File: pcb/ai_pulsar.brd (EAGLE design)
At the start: 30.5 x 30.5 mm, 24 parts, among them IC1 DS1307SO8-TIGHT, IC2 74HCT245MTC, J1 JST-3-MALE, J2 1X05, U1 MIC5205-3.3

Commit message: minor silkscreen fix
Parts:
- J1: value JST-3-MALE -> JST-3P-MALE
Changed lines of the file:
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@@
 <attribute name="NAME" x="22.70684375" y="7.712009375" size="0.8128" layer="26" ratio="10" rot="MR42"/>
 </element>
-<element name="J1" library="Ai_Connectors" package="JST-3P-SMD" value="JST-3-MALE" x="25.0952" y="15.24" smashed="yes" rot="MR90"/>
+<element name="J1" library="Ai_Connectors" package="JST-3P-SMD" value="JST-3P-MALE" x="25.0952" y="15.24" smashed="yes" rot="MR90"/>
 <element name="-" library="Ai_Connectors" package="1X01-PETAL" value="1X01-PETAL" x="6.985" y="25.4" smashed="yes" rot="R40"/>
 <element name="+" library="Ai_Connectors" package="1X01-PETAL" value="1X01-PETAL" x="15.494" y="2.032" smashed="yes" rot="R180"/>

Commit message: Updating
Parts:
- added C5: 100uF, Ai_Passives:CAP-POL-EIA3216
- D1: device Ai_DiscreteSemis:SOD-523 -> Ai_DiscreteSemis:SMA-403D
- U1: value MIC5205-3.3 -> MIC5219-3.3
- moved U$6 11.0 mm to (23.8, 23.6)
- moved D1 8.71 mm to (13.1, 27.3), flipped to the bottom, turned to 222 degrees
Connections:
- net 5V: now also C5.A
- net GND: now also C5.C
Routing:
- net N$5: track 8.68 -> 18.2 mm, vias 2 -> 1
- net 5V: track 57.3 -> 63.5 mm
- net N$1: track 18.8 -> 19.5 mm
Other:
- board text added: "v1.2"
- board text removed: "v1.1"

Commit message: updating
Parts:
- removed +, -, D: 1X01-PETAL, Ai_Connectors:1X01-PETAL
- removed D1: PMEG2010AEB, Ai_DiscreteSemis:SMA-403D
- removed IC2: 74HCT245MTC, Ai_IC:SSOP20
- added C10, C11, C12, C13, C14, C15, C16, C17, C18, C19, C20, C21, C22, C23, C24, C25, C26, C27, C28, C29, C6, C7, C8, C9: (no value), Ai_Passives:CAP-0603
- added F1: (no value), Ai_Passives:PTC-1206
- added JS1: 1X02-SJ-NO, Ai_Connectors:1X02-SJ-NO
- added JS2: 1X02-SJ-NC, Ai_Connectors:1X02-SJ-NC
- added LED1, LED10, LED11, LED12, LED13, LED14, LED15, LED16, LED17, LED18, LED19, LED2, LED20, LED21, LED22, LED23, LED24, LED3, LED4, LED5, LED6, LED7, LED8, LED9: LED-WS2812B-SM, Ai_LED:LED-WS2812B-SM
- added LED25, LED26: (no value), Ai_LED:LED-0603
- added Q1: BSS138, Ai_DiscreteSemis:SOT-23
- added R10, R11: 330, Ai_Passives:RES-0603
- added R6: 10K, Ai_Passives:RES-0603
- added R7, R8, R9: 1K, Ai_Passives:RES-0603
- added STANDOFF1, STANDOFF2, STANDOFF3, STANDOFF4: STAND-OFF4T, Ai_Electromechanical:STAND-OFF-4T
- added U2: FT231X-Q, Ai_IC:QFN20
- C1, C3: value 0.1uF -> 10uF
- C2: value 10uF -> 0.1uF
- C4: value 10uF -> (none)
- C5: value 100uF -> (none); device Ai_Passives:CAP-POL-EIA3216 -> Ai_Passives:CAP-0603
- J2: value 1X05 -> JST-2P-MALE; device Ai_Connectors:1X05 -> Ai_Connectors:JST-2P-SMD
- R1, R2: value 1K -> 22
- R5: value 1K -> 10K
- moved J2 50.0 mm to (52.7, 26.0), turned to 0 degrees
- moved USB1 49.7 mm to (38.9, 48.3), turned to 180 degrees
- moved C5 40.2 mm to (16.0, 45.2), flipped to the top, turned to 0 degrees
- moved J1 38.9 mm to (52.7, 42.7), flipped to the top, turned to 180 degrees
- moved C3 35.9 mm to (42.7, 22.9), turned to 270 degrees
- moved R1 35.9 mm to (28.4, 45.2), turned to 0 degrees
- moved R2 35.1 mm to (28.4, 43.7), turned to 0 degrees
- moved R3 32.8 mm to (45.7, 22.9), turned to 90 degrees
- moved C4 28.4 mm to (16.0, 43.7)
- moved C2 28.1 mm to (16.5, 39.4), turned to 270 degrees
- moved R4 26.6 mm to (18.0, 39.4)
- moved IC1 23.9 mm to (16.5, 30.5), flipped to the top, turned to 270 degrees
- moved C1 22.6 mm to (15.0, 39.4), turned to 90 degrees
- moved 3V-BATT 20.7 mm to (33.0, 17.8), flipped to the top, turned to 180 degrees
- moved U$6 20.7 mm to (34.3, 5.71), turned to 0 degrees
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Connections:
- removed net 3V3IO3: RFDUINO.4
- removed net 3V3IO4: RFDUINO.5
- removed net DTR: C1.2, J2.5
- removed net RESET: C1.1, RFDUINO.14
- removed net RXI: J2.4, R1.2
- removed net TXO: J2.3, R2.2
- new net !RST: C5.1, RFDUINO.14
- new net N$10: C5.2, U2.18
- new net N$11: LED26.C, R11.2
- new net N$12: LED25.C, R10.2
- new net N$14: R10.1, U2.14
- new net N$15: R11.1, U2.7
- new net N$17: JS1.2
- new net N$2: R1.2, USB1.D-
- new net N$30: JS2.1, LED1.4
- new net N$31: LED1.2, LED2.4
- new net N$6: R2.2, USB1.D+
- new net N$7: R9.1, U2.1
- new net N$8: R8.1, U2.17
- new net USBDM: R1.1, U2.9
- new net USBDP: R2.1, U2.8
- new net VCCIO: C4.2, LED25.A, LED26.A, U2.10, U2.11, U2.20
- net 3V3: now also C2.2, C3.1, Q1.1, R5.1; no longer C3.2, C4.1
- net 3V3IO2: now also Q1.2, R5.2; no longer IC2.2
- net 3V3IO5: no longer RFDUINO.6
- net 3V3IO6: no longer RFDUINO.7
- net 3V3RXD: now also R9.2; no longer R1.1
- net 3V3TXD: now also R8.2; no longer R2.1
- net 5V: now also C1.1, C6.2, C7.2, F1.2, LED1.1, LED2.1, LED3.1, R6.1, U2.12; no longer +.1, C2.1, C5.A, D1.C, IC2.1, IC2.20, J2.2
- net 5VIO2: now also Q1.3, R6.2, R7.2; no longer IC2.18, R5.2
- net D: now also JS1.1, JS2.2, R7.1; no longer D.1, R5.1
- net GND: now also C1.2, C2.1, C3.2, C4.1, C6.1, C7.1, LED1.3, LED2.3, U2.13, U2.21, U2.3; no longer -.1, C2.2, C3.1, C4.2, C5.C, IC2.10, IC2.19, J2.1
- net N$5: now also F1.1; no longer D1.A
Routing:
- net 5V: track 63.5 -> 0.00 mm, vias 4 -> 0
- net 3V3: track 31.2 -> 0.00 mm
- net 3V3IO6: track 26.5 -> 0.00 mm, vias 2 -> 0
- net 3V3IO5: track 24.3 -> 0.00 mm, vias 2 -> 0
- net N$1: track 19.5 -> 0.00 mm
- net 3V3IO2: track 19.5 -> 0.00 mm, vias 2 -> 0
- net 3V3TXD: track 18.4 -> 0.00 mm, vias 2 -> 0
- net N$5: track 18.2 -> 0.00 mm, vias 1 -> 0
- net N$4: track 17.5 -> 0.00 mm, vias 1 -> 0
- net D: track 17.1 -> 0.00 mm, vias 1 -> 0
- net DTR: track 13.2 -> 0.00 mm
- net RXI: track 11.6 -> 0.00 mm, vias 1 -> 0
- net 5VIO2: track 10.8 -> 0.00 mm
- net TXO: track 9.90 -> 0.00 mm
- net N$3: track 8.91 -> 0.00 mm, vias 1 -> 0
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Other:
- board size 30.5 x 30.5 mm -> 66 x 66 mm

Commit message: routing under way
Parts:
- added D1: DIODE-SCHOTTKY-DUAL, Ai_DiscreteSemis:SOT-23
- added D2: (no value), Ai_DiscreteSemis:SOD-523
- 3V-BATT: device Ai_Connectors:CR1220-SMD -> Ai_Connectors:CR1025-SMD
- moved C29 139.8 mm to (37.1, 63.9), turned to 82.5 degrees
- moved C28 139.0 mm to (29.0, 63.9), turned to 97.5 degrees
- moved C27 136.2 mm to (21.1, 61.8), turned to 112.5 degrees
- moved C26 126.1 mm to (14.1, 57.7), turned to 127.5 degrees
- moved C25 120.3 mm to (8.33, 52.0), turned to 142.5 degrees
- moved C24 113.3 mm to (4.27, 44.9), turned to 157.5 degrees
- moved C9 106.5 mm to (61.8, 44.9), turned to 22.5 degrees
- moved C10 104.8 mm to (63.9, 37.1), turned to 7.5 degrees
- moved C11 101.6 mm to (63.9, 29.0), turned to 352.5 degrees
- moved C23 101.2 mm to (2.16, 37.1), turned to 172.5 degrees
- moved C12 97.2 mm to (61.8, 21.1), turned to 337.5 degrees
- moved C22 93.2 mm to (2.16, 29.0), turned to 187.5 degrees
- moved C13 86.3 mm to (57.7, 14.1), turned to 322.5 degrees
- moved C21 85.8 mm to (4.27, 21.1), turned to 202.5 degrees
- moved C14 84.0 mm to (52.0, 8.33), turned to 307.5 degrees
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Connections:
- new net +: D2.A, J2.1
- new net DI-1: LED6.2, LED7.4
- new net DI-2: LED18.2, LED19.4
- new net N$13: LED12.2, LED13.4
- new net N$16: LED2.2, LED3.4
- new net N$18: LED3.2, LED4.4
- new net N$19: LED4.2, LED5.4
- new net N$20: LED5.2, LED6.4
- new net N$21: LED7.2, LED8.4
- new net N$22: LED8.2, LED9.4
- new net N$23: LED10.4, LED9.2
- new net N$24: LED10.2, LED11.4
- new net N$25: LED11.2, LED12.4
- new net N$26: LED13.2, LED14.4
- new net N$27: LED14.2, LED15.4
- new net N$28: LED15.2, LED16.4
- new net N$29: LED16.2, LED17.4
- new net N$32: LED17.2, LED18.4
- new net N$33: LED19.2, LED20.4
- new net N$34: LED20.2, LED21.4
- new net N$35: LED21.2, LED22.4
- new net N$36: LED22.2, LED23.4
- new net N$37: LED23.2, LED24.4
- new net VBAT: D1.2, D2.C
- new net VCC: C1.1, C10.2, C11.2, C12.2, C13.2, C14.2, C15.2, C16.2, C17.2, C18.2, C19.2, C20.2, C21.2, C22.2, C23.2, C24.2, C25.2, C26.2, C27.2, C28.2, C29.2, C6.2, C7.2, C8.2, C9.2, D1.3, IC1.8, LED1.1, LED10.1, LED11.1, LED12.1, LED13.1, LED14.1, LED15.1, LED16.1, LED17.1, LED18.1, LED19.1, LED2.1, LED20.1, LED21.1, LED22.1, LED23.1, LED24.1, LED3.1, LED4.1, LED5.1, LED6.1, LED7.1, LED8.1, LED9.1, R6.1, U1.1, U1.3, U2.12
- net 5V: now also D1.1; no longer C1.1, C6.2, C7.2, IC1.8, LED1.1, LED2.1, LED3.1, R6.1, U1.1, U1.3, U2.12
- net GND: now also C10.1, C11.1, C12.1, C13.1, C14.1, C15.1, C16.1, C17.1, C18.1, C19.1, C20.1, C21.1, C22.1, C23.1, C24.1, C25.1, C26.1, C27.1, C28.1, C29.1, C8.1, C9.1, J2.2, LED10.3, LED11.3, LED12.3, LED13.3, LED14.3, LED15.3, LED16.3, LED17.3, LED18.3, LED19.3, LED20.3, LED21.3, LED22.3, LED23.3, LED24.3, LED3.3, LED4.3, LED5.3, LED6.3, LED7.3, LED8.3, LED9.3
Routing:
- net VCC: track 0.00 -> 319.3 mm, vias 0 -> 24
- net N$1: track 0.00 -> 39.9 mm
- net D: track 0.00 -> 20.9 mm
- net 3V3: track 0.00 -> 16.3 mm
- net N$37: track 0.00 -> 14.6 mm, vias 0 -> 2
- net N$23: track 0.00 -> 14.6 mm, vias 0 -> 2
- net N$27: track 0.00 -> 14.5 mm, vias 0 -> 2
- net N$36: track 0.00 -> 14.5 mm, vias 0 -> 2
- net N$32: track 0.00 -> 14.5 mm, vias 0 -> 2
- net N$24: track 0.00 -> 14.5 mm, vias 0 -> 2
- net DI-2: track 0.00 -> 14.5 mm, vias 0 -> 2
- net N$29: track 0.00 -> 14.5 mm, vias 0 -> 2
- net N$22: track 0.00 -> 14.5 mm, vias 0 -> 2
- net N$25: track 0.00 -> 14.5 mm, vias 0 -> 2
- net N$28: track 0.00 -> 14.5 mm, vias 0 -> 2
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
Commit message: routed v1.3
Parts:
- removed JS1: 1X02-SJ-NO, Ai_Connectors:1X02-SJ-NO
- removed JS2: 1X02-SJ-NC, Ai_Connectors:1X02-SJ-NC
- removed U$6: AI-LOGOXS, Ai_Miscellany:AI-LOGO-XS
- added RNG: 1X02-SJ-NC, Ai_Connectors:1X02-SJ-NC
- added STR: 1X02-SJ-NO, Ai_Connectors:1X02-SJ-NO
- 3V-BATT: value CR1220 -> CR1025
- moved C2 12.5 mm to (11.6, 27.9)
- moved R4 10.3 mm to (21.8, 29.8), turned to 90 degrees
- moved C1 8.47 mm to (11.6, 31.6), turned to 270 degrees
- moved U1 6.53 mm to (19.4, 29.7)
- moved U$9 3.61 mm to (25.4, 7.59)
- moved R10 3.58 mm to (25.3, 48.8)
- moved R7 2.79 mm to (45.7, 30.7)
- moved F1 2.54 mm to (42.9, 30.7)
- moved USB1 1.78 mm to (37.1, 48.3)
- moved J1 0.57 mm to (52.2, 42.4)
- moved LED26 0.52 mm to (25.4, 46.6)
- moved C4 0.51 mm to (15.0, 45.1)
- moved C5 0.51 mm to (15.0, 46.6)
- moved IC1 0.51 mm to (15.0, 29.7)
- moved J2 0.51 mm to (52.7, 25.5)
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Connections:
- net D: now also RNG.2, STR.1; no longer JS1.1, JS2.2
- net N$17: now also STR.2; no longer JS1.2
- net N$30: now also RNG.1; no longer JS2.1
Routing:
- net VCC: track 319.3 -> 383.2 mm, vias 24 -> 29
- net 5V: track 0.00 -> 63.4 mm, vias 0 -> 4
- net +: track 0.00 -> 53.3 mm, vias 0 -> 2
- net 3V3IO6: track 0.00 -> 41.6 mm
- net 5VIO2: track 0.00 -> 40.0 mm, vias 0 -> 2
- net 3V3: track 16.3 -> 51.0 mm, vias 0 -> 2
- net 3V3TXD: track 0.00 -> 34.4 mm, vias 0 -> 2
- net !RST: track 0.00 -> 28.9 mm, vias 0 -> 2
- net 3V3RXD: track 0.00 -> 26.2 mm, vias 0 -> 2
- net D: track 20.9 -> 42.4 mm
- net N$5: track 0.00 -> 17.5 mm
- net 3V3IO2: track 2.26 -> 19.4 mm, vias 0 -> 2
- net VCCIO: track 8.01 -> 23.2 mm, vias 0 -> 3
- net N$2: track 0.00 -> 12.8 mm, vias 0 -> 2
- net N$6: track 0.00 -> 9.43 mm
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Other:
- outline, holes or cut-outs redrawn
- board text added: "(NC)"
- board text added: "(NO)"
- board text added: "BLE BLINKY"
- board text added: "CR1025"
- board text added: "https://acrobotic.com"
- board text added: "v1.3"
- board text removed: "5V"
- board text removed: "Airwire of coin-cell battery connected internally."
- board text removed: "CR1220 (RTC)"
- board text removed: "D"
- board text removed: "DTR"
- board text removed: "GND"
- board text removed: "RXD"
- board text removed: "TXD"
- board text removed: "v1.2"
- board text removed: "www.acrobotic.com"

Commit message: fiddling with cutouts
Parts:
- removed D2: (no value), Ai_DiscreteSemis:SOD-523
- removed Q1: BSS138, Ai_DiscreteSemis:SOT-23
- removed R5, R6: 10K, Ai_Passives:RES-0603
- R7: value 1K -> 330
- XL1: device Ai_FrequencyControl:CRYSTAL-CYL-2X6MM-SMT -> Ai_FrequencyControl:EPSON-MC146
- moved C3 20.9 mm to (21.8, 24.9), turned to 90 degrees
- moved R3 20.1 mm to (25.9, 19.3), turned to 0 degrees
- moved R4 13.6 mm to (25.9, 16.9), turned to 180 degrees
- moved U$9 10.00 mm to (30.0, 16.5)
- moved 3V-BATT 7.49 mm to (33.0, 10.3), turned to 0 degrees
- moved USB1 6.35 mm to (37.1, 41.9)
- moved R1 5.08 mm to (28.4, 40.1)
- moved R2 5.08 mm to (28.4, 38.6)
- moved R8 5.08 mm to (15.0, 43.1)
- moved U2 5.08 mm to (21.7, 39.0)
- moved C1 5.08 mm to (11.6, 26.5)
- moved C2 5.08 mm to (11.6, 22.9)
- moved R7 5.08 mm to (45.7, 25.7)
- moved RFDUINO 5.08 mm to (33.0, 27.9)
- moved C4 5.08 mm to (15.0, 40.0)
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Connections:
- removed net +: D2.A, J2.1
- removed net 5VIO2: Q1.3, R6.2, R7.2
- new net 3V3IO3: RFDUINO.4
- new net 3V3IO4: RFDUINO.5
- net 3V3: no longer Q1.1, R5.1
- net 3V3IO2: now also R7.2; no longer Q1.2, R5.2
- net 3V3IO5: now also RFDUINO.6
- net 3V3IO6: now also RFDUINO.7
- net N$3: now also XL1.P$1; no longer XL1.1
- net N$4: now also XL1.P$2; no longer XL1.2
- net VBAT: now also J2.1; no longer D2.C
- net VCC: no longer R6.1
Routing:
- net +: track 53.3 -> 0.00 mm, vias 2 -> 0
- net VBAT: track 1.64 -> 52.7 mm, vias 0 -> 2
- net 5VIO2: track 40.0 -> 0.00 mm, vias 2 -> 0
- net 3V3IO5: track 9.97 -> 43.8 mm
- net 3V3: track 51.0 -> 42.0 mm, vias 2 -> 4
- net 3V3IO2: track 19.4 -> 10.7 mm, vias 2 -> 0
- net VCC: track 383.2 -> 390.8 mm
- net 5V: track 63.4 -> 70.6 mm
- net D: track 42.4 -> 47.3 mm
- net N$5: track 17.5 -> 13.7 mm
- net N$3: track 7.57 -> 4.80 mm
- net N$6: track 9.43 -> 9.96 mm
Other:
- outline, holes or cut-outs redrawn
- board text added: "v1.4"
- board text removed: "v1.3"

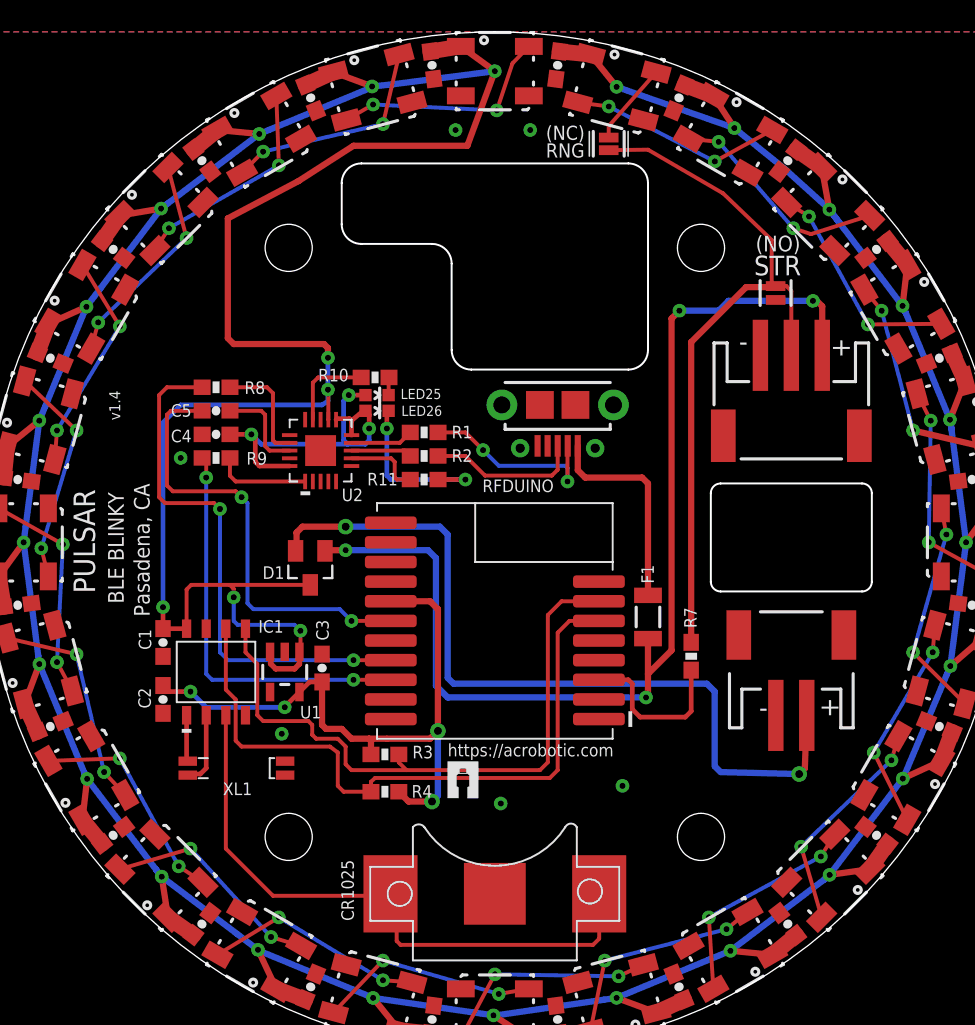
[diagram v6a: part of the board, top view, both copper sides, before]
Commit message: bigger cutout for micro-B connector
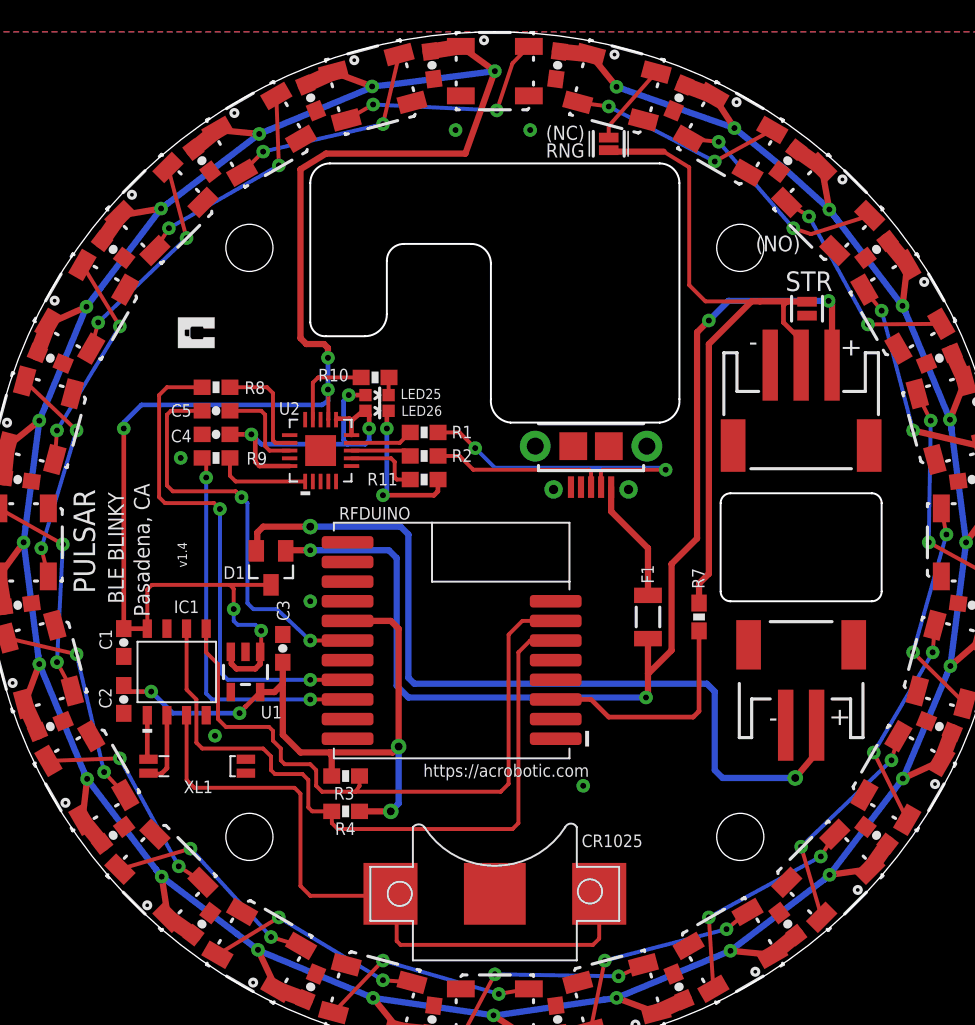
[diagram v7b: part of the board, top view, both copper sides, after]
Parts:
- C4, C5: value (none) -> 0.1uF
- moved U$9 32.8 mm to (14.9, 45.6), turned to 90 degrees
- moved USB1 3.43 mm to (39.2, 39.2)
- moved RFDUINO 3.07 mm to (30.2, 26.7)
- moved R3 2.90 mm to (23.4, 17.9)
- moved C3 2.84 mm to (19.3, 26.2)
- moved R4 2.84 mm to (23.4, 15.6)
- moved R7 2.59 mm to (46.2, 28.2)
- moved XL1 2.54 mm to (13.7, 18.5)
- moved STANDOFF3 2.54 mm to (48.9, 14.0)
- moved STANDOFF4 2.54 mm to (48.9, 52.1)
- moved U1 2.54 mm to (16.9, 24.6)
- moved C1 2.54 mm to (9.02, 26.5)
- moved C2 2.54 mm to (9.02, 22.9)
- moved IC1 2.54 mm to (12.4, 24.6)
- moved D1 2.54 mm to (18.5, 31.4)
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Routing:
- net N$2: track 12.5 -> 21.0 mm
- net VCC: track 390.8 -> 384.0 mm
- net N$5: track 13.7 -> 7.99 mm
- net 3V3IO2: track 10.7 -> 15.1 mm
- net N$1: track 40.1 -> 43.5 mm
- net 3V3IO5: track 43.8 -> 46.7 mm
- net VBAT: track 52.7 -> 55.2 mm
- net 5V: track 70.6 -> 73.0 mm
- net !RST: track 28.9 -> 26.6 mm
- net 3V3: track 42.0 -> 43.7 mm
- net 3V3TXD: track 34.4 -> 32.9 mm
- net 3V3RXD: track 26.2 -> 24.7 mm
- net N$6: track 9.96 -> 11.3 mm
- net N$11: track 11.2 -> 10.0 mm
- net 3V3IO6: track 41.8 -> 42.7 mm
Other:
- outline, holes or cut-outs redrawn
